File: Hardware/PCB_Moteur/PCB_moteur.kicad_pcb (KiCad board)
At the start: 2 copper layers, 60 x 105 mm, 194 parts, among them J1 XT30PW-F, J10 Conn_01x02, J11 Conn_01x02, J12 Conn_01x02, J13 Conn_01x02, J14 Conn_01x02, J15 Conn_01x02, J16 Conn_01x06_Pin, J17 Screw_Terminal_01x04, J18 Screw_Terminal_01x04, J19 Screw_Terminal_01x04, J2 Conn_01x06_Pin, J20 BM03B-GHS-TBT, J21 BM03B-GHS-TBT, J22 BM03B-GHS-TBT, J23 BM03B-GHS-TBT, J7 Conn_01x02, J8 Conn_01x02, J9 Conn_01x02, Q1 SI5442DU-T1-GE3, Q2 SI5442DU-T1-GE3, Q3 MMBT3904, Q4 SI7617DN-T1-GE3, U1 L6981N33DR, U2 STM32F103CBT6, U3 MCP1802T-5002I/OT, U4 LSF0204PWR, U5 ISOW1044, U6 LM393, U7 INA125UA/2K5, U8 INA125UA/2K5, U9 MAX6612MXK

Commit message: refactor: merge emile + main branches
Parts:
- added G***: LOGO, LOGO, B.Cu at (96.4, 47.4)
- added G***: LOGO, LOGO, B.Cu at (97.2, 124.2)
- added G***: LOGO, LOGO, B.Cu at (131.1, 47.3)
- added G***: LOGO, LOGO, B.Cu at (128.8, 124.1)
- added R61: 10k, Resistor_SMD:R_0805_2012Metric, F.Cu at (101.1, 75.0)
- moved R25 13.6 mm to (99.8, 100.4), turned to 180 degrees
- moved R26 6.04 mm to (95.0, 100.2), turned to 90 degrees
- moved R2 0.70 mm to (130.2, 60.0)
- moved R1 0.69 mm to (130.2, 62.0)
- moved C4 0.67 mm to (130.2, 64.2)
- moved C17 0.20 mm to (119.8, 72.2), turned to 90 degrees
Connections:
- C23 pad 1: 3V3_Main -> SYS_NRST
- J2 pad 6: 3V3_Main -> SYS_NRST
- U2 pad 7: 3V3_Main -> SYS_NRST
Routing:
- net VIN_Filtered: track 0.65 -> 8.83 mm
- net Servo2_Open: track 80.0 -> 77.1 mm
- net SYS_NRST: track 0.00 -> 2.44 mm
- net Servo1_Open: track 44.5 -> 43.5 mm
- net Vin_An: track 36.5 -> 37.2 mm
- added copper zone on F.Cu, net +5Viso
- added copper zone on F.Cu, net 3V3_Main
- added copper zone on B.Cu, net GND_iso
- added copper zone on B.Cu, net LC_IN-
- added copper zone on F.Cu, net VIN_Filtered

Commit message: wip: trace width
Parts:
- moved C17 0.18 mm to (119.9, 72.2)
- moved C16 0.09 mm to (119.9, 79.8)
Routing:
- net Servo4_Open: track 48.8 -> 49.7 mm, vias 1 -> 0
- net Servo3_Close: track 35.1 -> 35.9 mm, vias 1 -> 0
- net Servo4_Close: track 40.5 -> 41.3 mm, vias 1 -> 0
- net 3V3_An: track 30.8 -> 31.5 mm
- net Servo3_Open: track 43.9 -> 43.8 mm, vias 1 -> 0

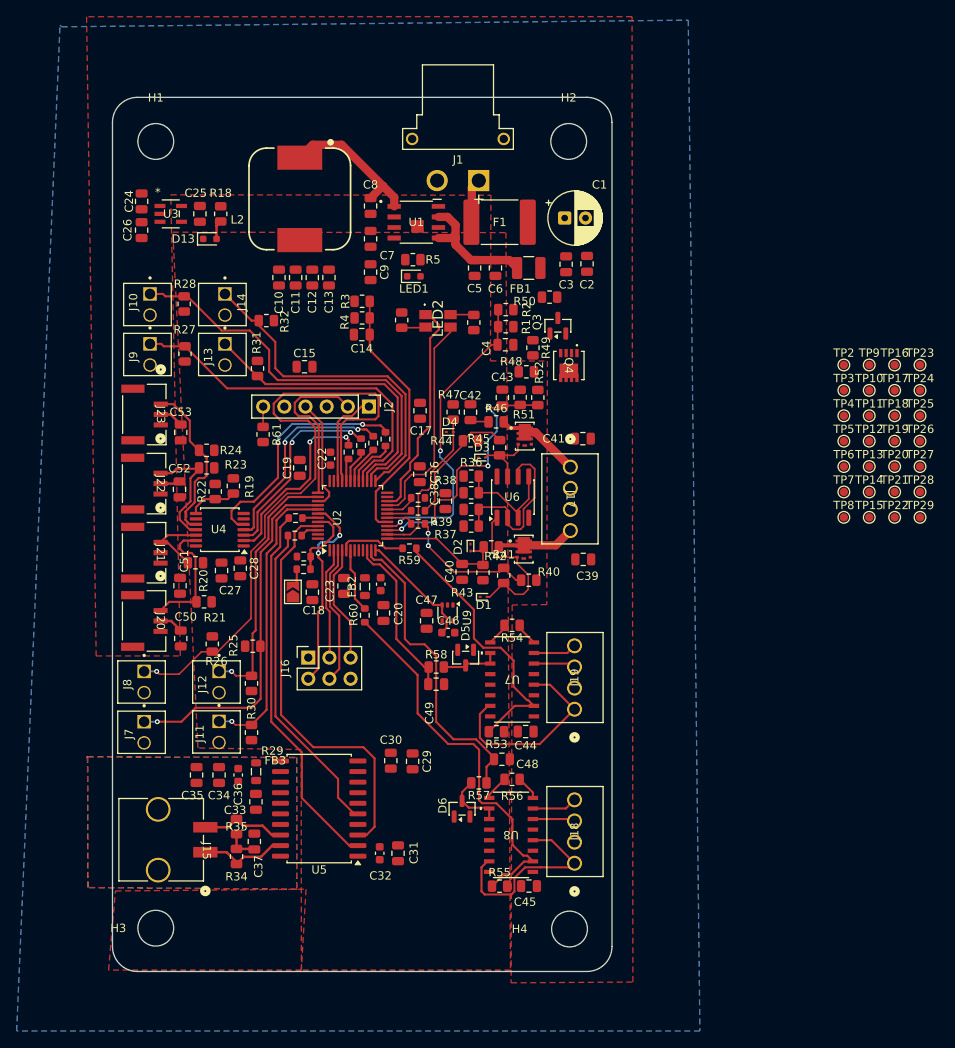
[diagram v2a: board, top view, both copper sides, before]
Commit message: wip: changement trace width et début GND Via
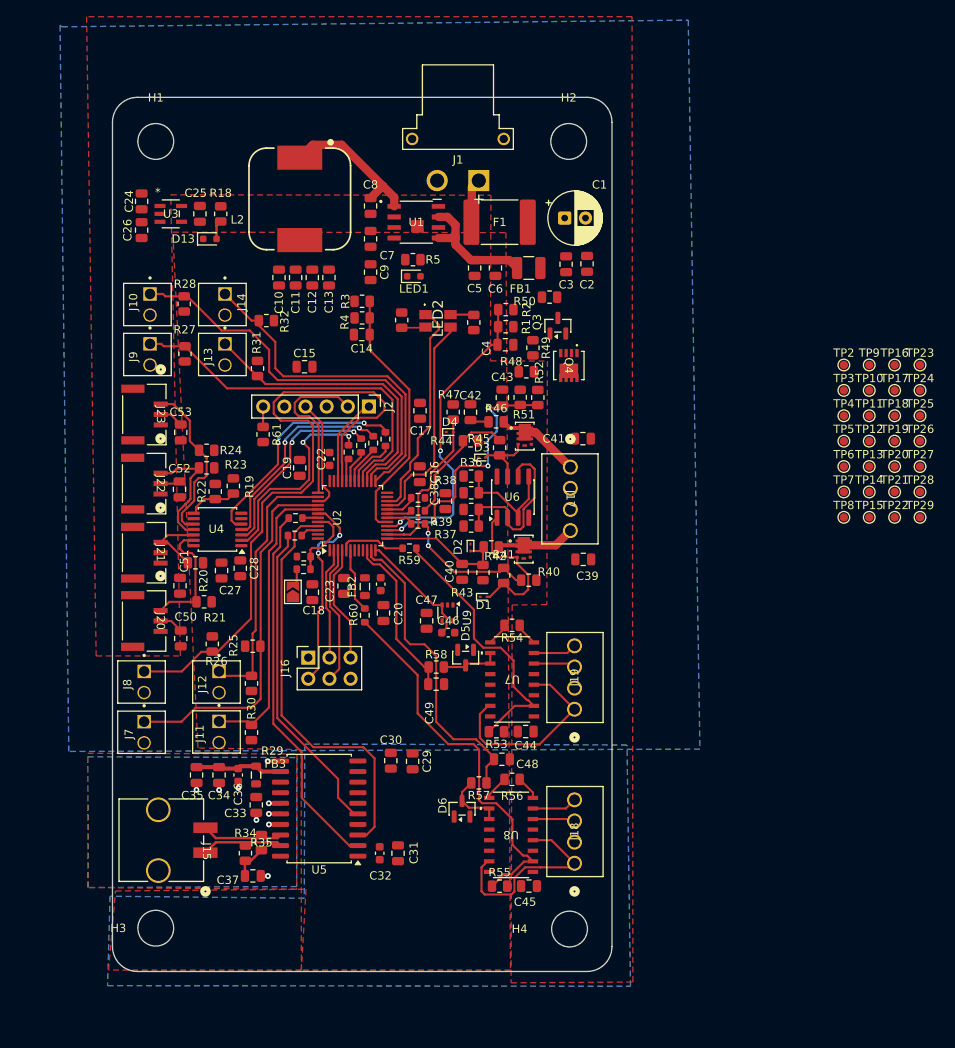
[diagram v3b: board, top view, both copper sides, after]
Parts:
- moved C37 4.13 mm to (99.9, 128.0), turned to 0 degrees
- moved R35 3.55 mm to (100.9, 124.0)
- moved R34 1.14 mm to (99.0, 125.3), turned to 90 degrees
- moved FB3 0.40 mm to (100.2, 115.9)
- moved C33 0.37 mm to (100.3, 119.5)
- moved U4 0.28 mm to (95.6, 86.4)
- moved C22 0.11 mm to (109.1, 77.9)
- moved J15 0.06 mm to (88.9, 123.7)
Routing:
- net +5VAiso: track 0.00 -> 10.5 mm
- net GND_iso: track 0.00 -> 10.4 mm, vias 0 -> 9
- net Servo1_PWM: track 22.8 -> 25.0 mm
- net SYS_SWDIO: track 11.6 -> 10.7 mm
- net Servo2_Close: track 31.0 -> 31.8 mm, vias 1 -> 0
- net Servo4_PWM: track 29.2 -> 28.6 mm
- net Servo4_Stepup: track 20.0 -> 20.7 mm
- net Servo2_Open: track 77.1 -> 77.6 mm, vias 1 -> 0
- net Servo1_Open: track 43.5 -> 44.0 mm, vias 1 -> 0
- net Servo1_Close: track 35.4 -> 35.6 mm, vias 1 -> 0

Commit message: wip: via
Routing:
- net LC_IN-: track 0.00 -> 26.5 mm, vias 0 -> 26
